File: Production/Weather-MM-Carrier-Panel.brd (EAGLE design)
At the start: 175 x 131.1 mm, 629 parts, among them J11 microSD, J13 RJ11 - WIND, J15 MICROMOD-2222-C, J16 QWIIC_RIGHT_ANGLE, J17 JTAG, J19 microSD, J2 JTAG, J24 RJ11 - RAIN, J25 RJ11 - WIND, J26 MICROMOD-2222-C, J3 QWIIC_RIGHT_ANGLE, J30 QWIIC_RIGHT_ANGLE, J31 JTAG, J33 microSD, J38 RJ11 - RAIN, J39 RJ11 - WIND, J40 MICROMOD-2222-C, J44 QWIIC_RIGHT_ANGLE, J45 JTAG, J47 microSD, J52 RJ11 - RAIN, J53 RJ11 - WIND, J54 MICROMOD-2222-C, J7 RJ11 - RAIN, U1 BME280, U10 BME280, U11 VEML6075, U12 AS3935, U13 AP7361C-33FGEUDFN-8, U14 BME280, U15 VEML6075, U16 AS3935, U2 VEML6075, U3 AS3935, U4 AP7361C-33FGEUDFN-8, U5 AP7361C-33FGEUDFN-8, U6 BME280, U7 VEML6075, U8 AS3935, U9 AP7361C-33FGEUDFN-8

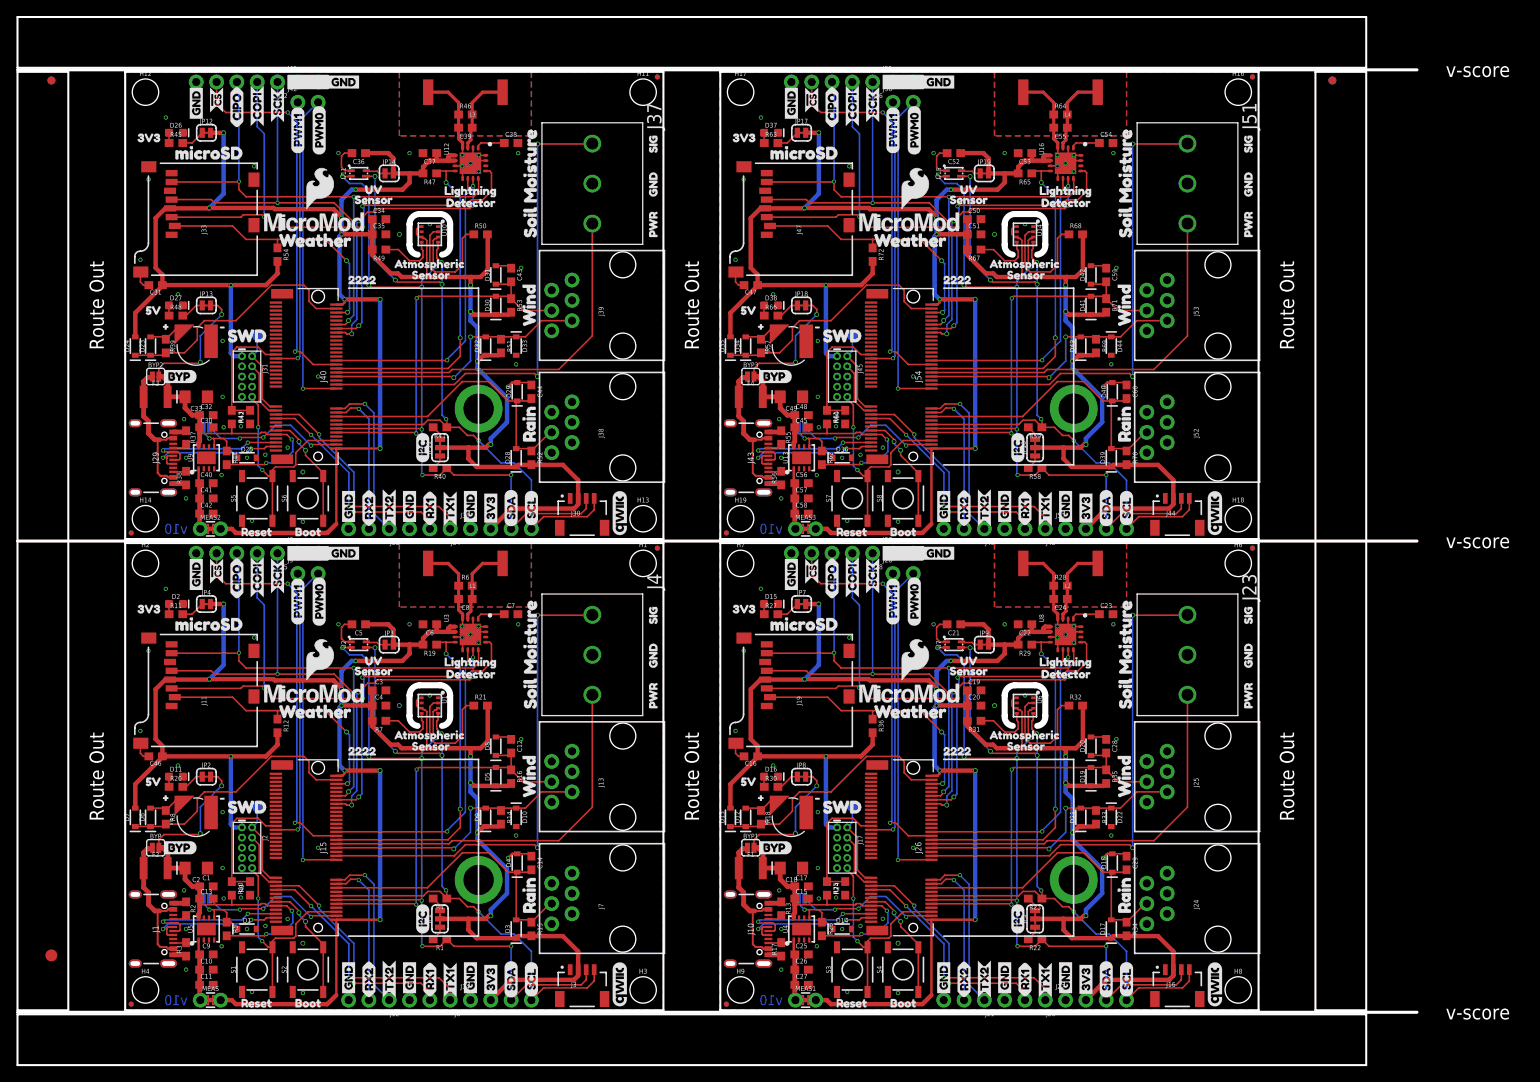
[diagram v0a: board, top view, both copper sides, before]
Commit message: Implemented SPI bus changes
Re-panelized and new gerbers
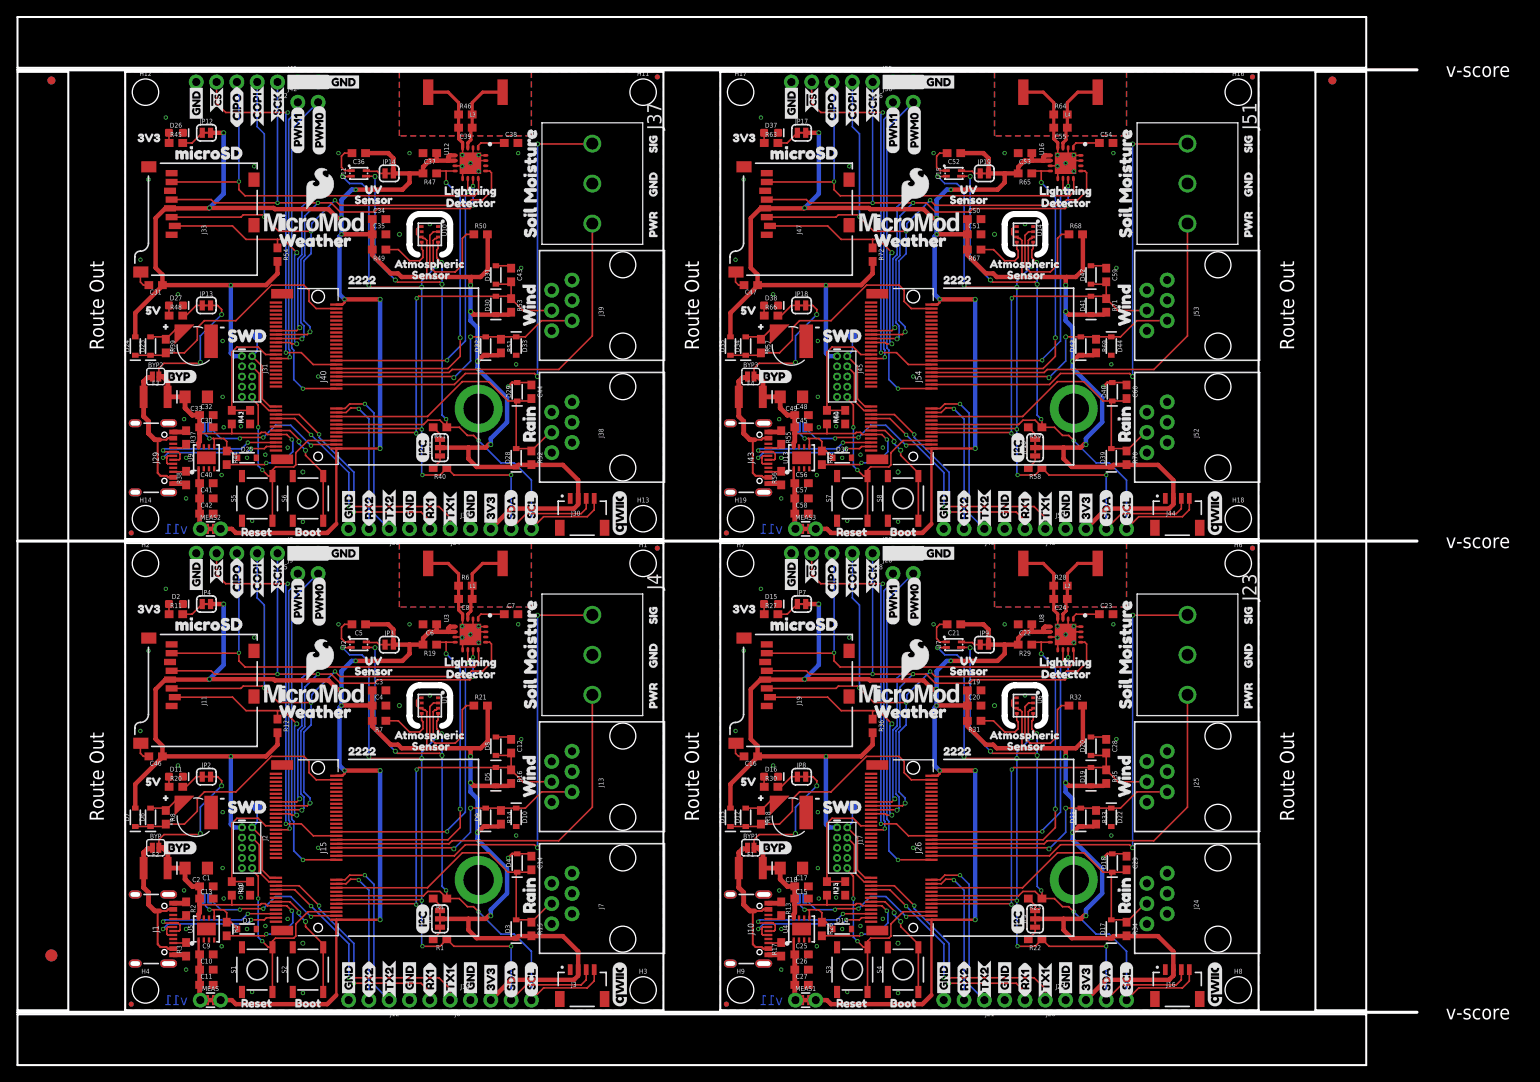
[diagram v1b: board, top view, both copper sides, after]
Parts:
- added E$6: (no value), SparkFun-Retired:FIDUCIAL-1.5X3
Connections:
- net SD_!CS!: now also J15.55; no longer J15.70
- net SD_!CS!1: now also J26.55; no longer J26.70
- net SD_!CS!2: now also J40.55; no longer J40.70
- net SD_!CS!3: now also J54.55; no longer J54.70
- net SPI_CIPO: now also J15.61; no longer J15.64
- net SPI_CIPO1: now also J26.61; no longer J26.64
- net SPI_CIPO2: now also J40.61; no longer J40.64
- net SPI_CIPO3: now also J54.61; no longer J54.64
- net SPI_COPI: now also J15.59; no longer J15.62
- net SPI_COPI1: now also J26.59; no longer J26.62
- net SPI_COPI2: now also J40.59; no longer J40.62
- net SPI_COPI3: now also J54.59; no longer J54.62
- net SPI_SCK: now also J15.57; no longer J15.60
- net SPI_SCK1: now also J26.57; no longer J26.60
- net SPI_SCK2: now also J40.57; no longer J40.60
- net SPI_SCK3: now also J54.57; no longer J54.60
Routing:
- net SPI_SCK1: track 74.5 -> 78.6 mm
- net SPI_SCK3: track 74.5 -> 78.6 mm
- net SPI_SCK: track 74.5 -> 78.6 mm
- net SPI_SCK2: track 74.5 -> 78.6 mm
- net SPI_CIPO: track 71.8 -> 74.7 mm
- net SPI_CIPO3: track 71.8 -> 74.7 mm
- net SPI_CIPO2: track 71.8 -> 74.7 mm
- net SPI_CIPO1: track 71.8 -> 74.7 mm
- net SPI_COPI: track 80.2 -> 82.1 mm
- net SPI_COPI3: track 80.2 -> 82.1 mm
- net SPI_COPI1: track 80.2 -> 82.1 mm
- net SPI_COPI2: track 80.2 -> 82.1 mm
- net PWM6: track 40.8 -> 42.0 mm
- net PWM2: track 40.8 -> 42.0 mm
- net PWM4: track 40.8 -> 42.0 mm
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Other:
- board text added: "v11"
- board text removed: "v10"
